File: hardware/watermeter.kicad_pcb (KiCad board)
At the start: 2 copper layers, 105 x 90 mm, 72 parts, among them J1 Screw_Terminal_01x03, J10 flow_meter, J11 USB-TYPE-C-31-M-12, J2 Screw_Terminal_01x03, J3 Conn_01x08_Pin, J4 Conn_01x06_Shielded, J5 24V_Power, J6 PWM_IN, J7 PWM_OUT, J8 DHT21, J9 Conn_01x06_Shielded, K1 SRD-05VDC-SL-C, K2 SRD-05VDC-SL-C, Q1 NPN, Q2 NPN, SW1 Reboot, U1 ESP32-C6-MINI-1, U2 USBLC6-2SC6, U3 LM3671MFX-3.3/NOPB, U4 K7805-500R3

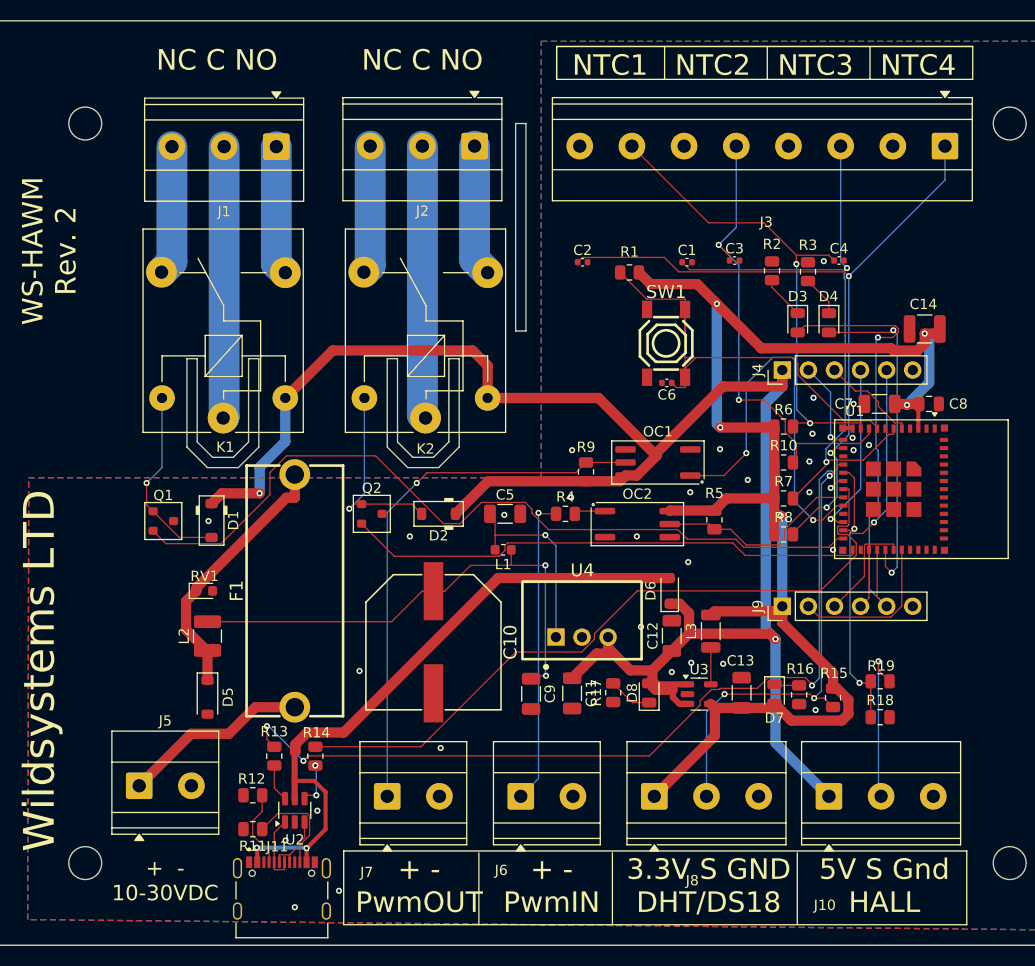
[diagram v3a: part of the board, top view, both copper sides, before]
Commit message: Board V2. fix: power supply fix: NTC noise suppression fix: Q1 and Q2 wrong pin numbers fix: Increased power trice width
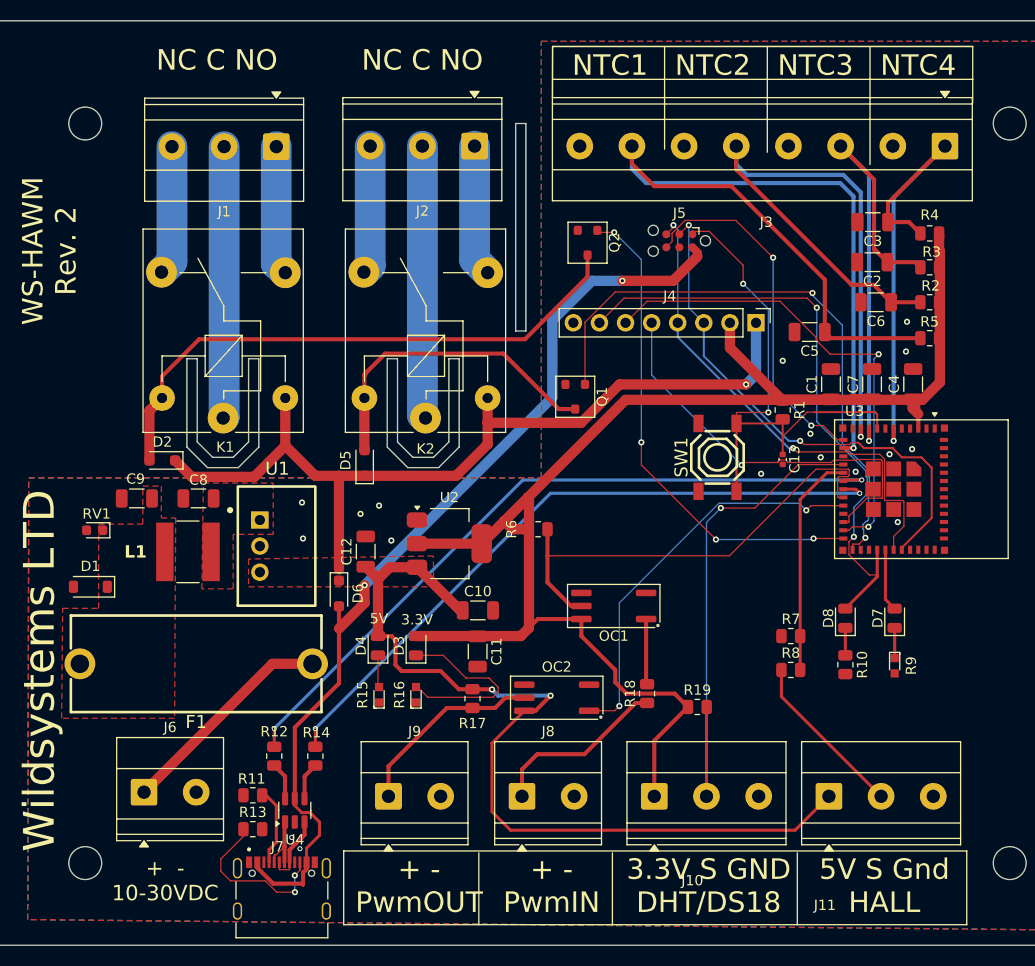
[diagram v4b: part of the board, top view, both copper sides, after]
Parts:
- removed C14: 49uF/16V, Capacitor_SMD:C_1210_3225Metric
- removed the J7 at (124.9, 126.5)
- removed L2: FHW1210IF820JST, Inductor_SMD:L_1210_3225Metric
- removed L3: 2.2uH, Inductor_SMD:L_1206_3216Metric
- removed the R17 at (146.9, 116.4)
- removed the R18 at (172.9, 118.8)
- removed the R6 at (163.5, 90.5)
- removed the U3 at (155.3, 116.5)
- removed the U4 at (143.9, 111.0)
- added J8: Screw_Terminal_01x02, TerminalBlock_Phoenix:TerminalBlock_Phoenix_MKDS-1,5-2-5.08_1x02_P5.08mm_Horizontal, F.Cu at (138.0, 126.5)
- added R4: 4k7, Resistor_SMD:R_0805_2012Metric, F.Cu at (177.7, 71.7)
- added R5: 4k7, Resistor_SMD:R_0805_2012Metric, F.Cu at (177.7, 81.9)
- added R9: 270R, Digikey library:LED_0603, F.Cu at (174.3, 113.8)
- added U1: R-78E5.0-1.0, MyFootprints:PWRM-TH_K78XX-500R3, F.Cu at (112.5, 102.1)
- added U2: ZLDO1117G33TA, Package_TO_SOT_SMD:SOT-223-3_TabPin2, F.Cu at (130.9, 101.9)
- C1: value 0.1uF -> 47uF/16V; footprint Capacitor_SMD:C_0402_1005Metric -> Capacitor_SMD:C_1206_3216Metric
- C10: value 680uF/50V -> 10uF/50V; footprint MyFootprints:CAP-SMD_BD12.5-L13.0-W13.0-LS14.4-FD -> Capacitor_SMD:C_1206_3216Metric
- C11: value 22uF/10V -> 22uF
- C12: value 10uF/10V -> 22uF
- C13: value 10uF/10V -> 1uF; footprint Capacitor_SMD:C_1206_3216Metric -> Capacitor_SMD:C_0402_1005Metric
- C2, C3: footprint Capacitor_SMD:C_0402_1005Metric -> Capacitor_SMD:C_1206_3216Metric
- C4: value 0.1uF -> 10uF/50V; footprint Capacitor_SMD:C_0402_1005Metric -> Capacitor_SMD:C_1206_3216Metric
- C5: value 10uF/50V -> 0.1uF
- C6: value 1uF -> 0.1uF; footprint Capacitor_SMD:C_0402_1005Metric -> Capacitor_SMD:C_1206_3216Metric
- C7: value 10uF/10V -> 0.1uF
- C8: value 0.1uF/6.3v -> 10uF/50V; footprint Capacitor_SMD:C_0805_2012Metric -> Capacitor_SMD:C_1206_3216Metric
- C9: value 4.7uF/63V -> 10uF/50V
- D2: renamed from D1; footprint PCM_Diode_SMD_AKL:D_SOD-123 -> Diode_SMD:D_SOD-323_HandSoldering
- D3: value KT-0805B -> KT-0805G; footprint Diode_SMD:D_0805_2012Metric -> LED_SMD:LED_0805_2012Metric
- D5: renamed from D2; footprint PCM_Diode_SMD_AKL:D_SOD-123 -> Diode_SMD:D_SOD-323_HandSoldering
- D8: value KT-0805G -> KT-0805B; footprint LED_SMD:LED_0805_2012Metric -> Diode_SMD:D_0805_2012Metric
- J10: renamed from J8; value DHT21 -> SRD-05VDC-SL-C
- J11: renamed from J10; value flow_meter -> SRD-05VDC-SL-C
- J4: value Conn_01x06_Shielded -> Conn_01x08_Pin; footprint Connector_PinHeader_2.54mm:PinHeader_1x06_P2.54mm_Vertical -> Connector_PinHeader_2.54mm:PinHeader_1x08_P2.54mm_Vertical
- J5: value 24V_Power -> TC2030; footprint TerminalBlock_Phoenix:TerminalBlock_Phoenix_MKDS-1,5-2-5.08_1x02_P5.08mm_Horizontal -> Connector:Tag-Connect_TC2030-IDC-NL_2x03_P1.27mm_Vertical
- J6: value PWM_IN -> Screw_Terminal_01x02
- J9: value Conn_01x06_Shielded -> Screw_Terminal_01x02; footprint Connector_PinHeader_2.54mm:PinHeader_1x06_P2.54mm_Vertical -> TerminalBlock_Phoenix:TerminalBlock_Phoenix_MKDS-1,5-2-5.08_1x02_P5.08mm_Horizontal
- L1: value 22uH -> 12uH; footprint Inductor_SMD:L_0603_1608Metric -> MyFootprints:IND_ASPI-6045S-120M-T
- Q1, Q2: value NPN -> PDTD123YK; footprint PCM_Package_TO_SOT_SMD_AKL:SOT-23 -> PCM_Package_TO_SOT_SMD_AKL:SC-59
- R10: value 4k7 -> 15R
- R15: value 10K -> 270R; footprint Resistor_SMD:R_0805_2012Metric -> Digikey library:LED_0603
- R16: value 20R -> 270R; footprint Resistor_SMD:R_0805_2012Metric -> Digikey library:LED_0603
- R19: value 1k -> 10K
- R2: value 15R -> 4k7
- R3: value 20R -> 4k7
- R7: value 4k7 -> 2k
- R8: value 4k7 -> 1k
- moved J5 74.7 mm to (153.3, 72.4), turned to 180 degrees
- moved C8 71.7 mm to (106.5, 97.5), turned to 180 degrees
- moved D4 54.0 mm to (124.0, 111.8), turned to 90 degrees
- moved D3 48.7 mm to (127.7, 111.8), turned to 90 degrees
- moved R15 44.2 mm to (124.1, 116.6), turned to 90 degrees
- moved C9 42.8 mm to (100.5, 97.5), turned to 180 degrees
- moved J9 42.6 mm to (125.0, 126.5), turned to 0 degrees
- moved Q1 41.9 mm to (143.2, 87.6), turned to -90 degrees
- moved R16 37.3 mm to (127.7, 116.6)
- moved J6 36.7 mm to (101.2, 126.1)
- moved C5 34.5 mm to (166.0, 81.3), turned to 180 degrees
- moved Q2 33.7 mm to (144.4, 72.6), turned to -90 degrees
- moved D6 32.2 mm to (120.2, 106.8), turned to -90 degrees
- moved C12 30.9 mm to (122.8, 102.7)
- moved L1 30.7 mm to (105.5, 102.7), turned to 0 degrees
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- renumbered D5 to D1, J11 to J7, OC2 to OC1, OC1 to OC2, R12 to R11, R13 to R12, R11 to R13, R9 to R17, R4 to R18, R5 to R6, U1 to U3, U2 to U4
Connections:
- C1 pad 1: /IO3 -> +3.3V
- C10 pad 1: Net-(C10-Pad1) -> +5V
- C11 pad 1: +5V -> +3.3V
- C13 pad 1: +3.3V -> /EN
- C2 pad 1: /IO1 -> /IO4
- C3 pad 1: /IO4 -> /IO3
- C4 pad 1: /IO5 -> +3.3V
- C5 pad 1: Net-(U4-IN) -> /IO1
- C6 pad 1: Net-(U1-EN) -> /IO5
- C8 pad 1: +3.3V -> Net-(U4-IN)
- C9 pad 1: Net-(C10-Pad1) -> /24V_FUSED
- D3 pad 1: Net-(D3-K) -> Net-(D7-K)
- D3 pad 2: /IO22 -> +3.3V
- D4 pad 1: Net-(D4-K) -> Net-(D8-K)
- D4 pad 2: /IO23 -> +5V
- D7 pad 1: Net-(D7-K) -> Net-(D4-K)
- D7 pad 2: +3.3V -> /IO23
- D8 pad 1: Net-(D8-K) -> Net-(D3-K)
- D8 pad 2: +5V -> /IO22
- J3 pad 1: /IO1 -> /IO3
- J3 pad 3: /IO3 -> /IO4
- J3 pad 5: /IO4 -> /IO5
- J3 pad 7: /IO5 -> /IO1
- J4 pad 2: /IO0 -> +3.3V
- J4 pad 3: /IO2 -> /TXD0
- J4 pad 4: /IO8 -> /RXD0
- J4 pad 5: /IO9 -> /IO8
- J4 pad 6: GND -> /IO9
- J5 pad 1: /Power/24V -> /EN
- J5 pad 2: GND -> /5V_USB
- J6 pad 1: Net-(J6-Pin_1) -> /Power/24V
- J9 pad 1: +3.3V -> Net-(J7-Pin_1)
- J9 pad 2: /TXD0 -> GND
- L1 pad 1: Net-(C10-Pad1) -> /24V_FUSED
- Q1 pad 1: Net-(D1-A) -> /IO19
- Q1 pad 2: /IO18 -> GND
- Q1 pad 3: GND -> Net-(D2-A)
- Q2 pad 1: Net-(D2-A) -> /IO18
- Q2 pad 2: /IO19 -> GND
- Q2 pad 3: GND -> Net-(D1-A)
- R1 pad 2: Net-(U1-EN) -> /EN
- R10 pad 1: +3.3V -> Net-(D3-K)
- R10 pad 2: /IO4 -> GND
- R15 pad 1: +3.3V -> GND
- R15 pad 2: /IO6 -> Net-(D8-K)
- R19 pad 1: Net-(J10-Pin_2) -> +3.3V
- R19 pad 2: /IO7 -> /IO6
- R2 pad 1: Net-(D3-K) -> +3.3V
- R2 pad 2: GND -> /IO5
- R3 pad 1: Net-(D4-K) -> +3.3V
- R3 pad 2: GND -> /IO4
- R7 pad 1: +3.3V -> /IO7
- R7 pad 2: /IO3 -> GND
- R8 pad 1: +3.3V -> Net-(J10-Pin_2)
- R8 pad 2: /IO1 -> /IO7
- SW1 pad 2: Net-(U1-EN) -> /EN
- U3 pad 8: Net-(U1-EN) -> /EN
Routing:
- net /EN: track 0.00 -> 55.6 mm, vias 0 -> 2
- net Net-(C10-Pad1): track 49.0 -> 0.00 mm, vias 2 -> 0
- net Net-(U1-EN): track 44.5 -> 0.00 mm
- net /RXD0: track 10.6 -> 48.3 mm, vias 0 -> 2
- net Net-(D1-A): track 18.7 -> 56.2 mm, vias 1 -> 0
- net /TXD0: track 15.5 -> 50.7 mm, vias 0 -> 2
- net Net-(J7-Pin_1): track 52.8 -> 18.9 mm, vias 1 -> 0
- net /IO18: track 78.5 -> 48.1 mm, vias 0 -> 4
- net /IO9: track 18.9 -> 47.6 mm, vias 1 -> 2
- net /5V_USB: track 65.9 -> 93.1 mm
- net /IO23: track 32.8 -> 6.10 mm, vias 2 -> 0
- net /IO14: track 20.2 -> 46.5 mm
- net /IO0: track 8.78 -> 35.0 mm, vias 1 -> 2
- net /24V_FUSED: track 25.8 -> 0.00 mm
- net /IO8: track 17.1 -> 40.5 mm
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- added copper zone on F.Cu, net +5V
- added copper zone on F.Cu, net /24V_FUSED
- added copper zone on F.Cu, net Net-(U4-IN)
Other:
- board text added: "3.3V"
- board text added: "5V"
- board text added: "5V 3.3V TXD0 RXD0 IO8 IO9 IO22 GND"
- board text removed: "+3.3v TXD0 RXD0 IO21 IO22 GND"
- board text removed: "+5V IO0 IO2 IO8 IO9 GND"
- board text removed: "Pin Function IO0 EXT_IO0 IO1 EXT_IO1 IO2 EXT_IO2 IO3 DHT21/DS18 IO4 NTC1 IO5 FLOW IO6 PWM_IN IO7 NTC2 IO8 PWM_OUT IO9 EXT_IO9 IO18 RELAY1 IO19 RELAY2 IO22 LED1 IO23 LED2"
